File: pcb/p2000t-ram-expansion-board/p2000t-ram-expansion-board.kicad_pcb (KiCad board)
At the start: 2 copper layers, 110 x 68.1 mm, 28 parts, among them J1 EXPANSION BOARD, J2 POWER, J3 TERMINAL, U1 74HC04, U2 CY62256-70PC, U3 74HC00, U4 CY62256-70PC, U5 74HC688, U6 74HC32, U7 74HC173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

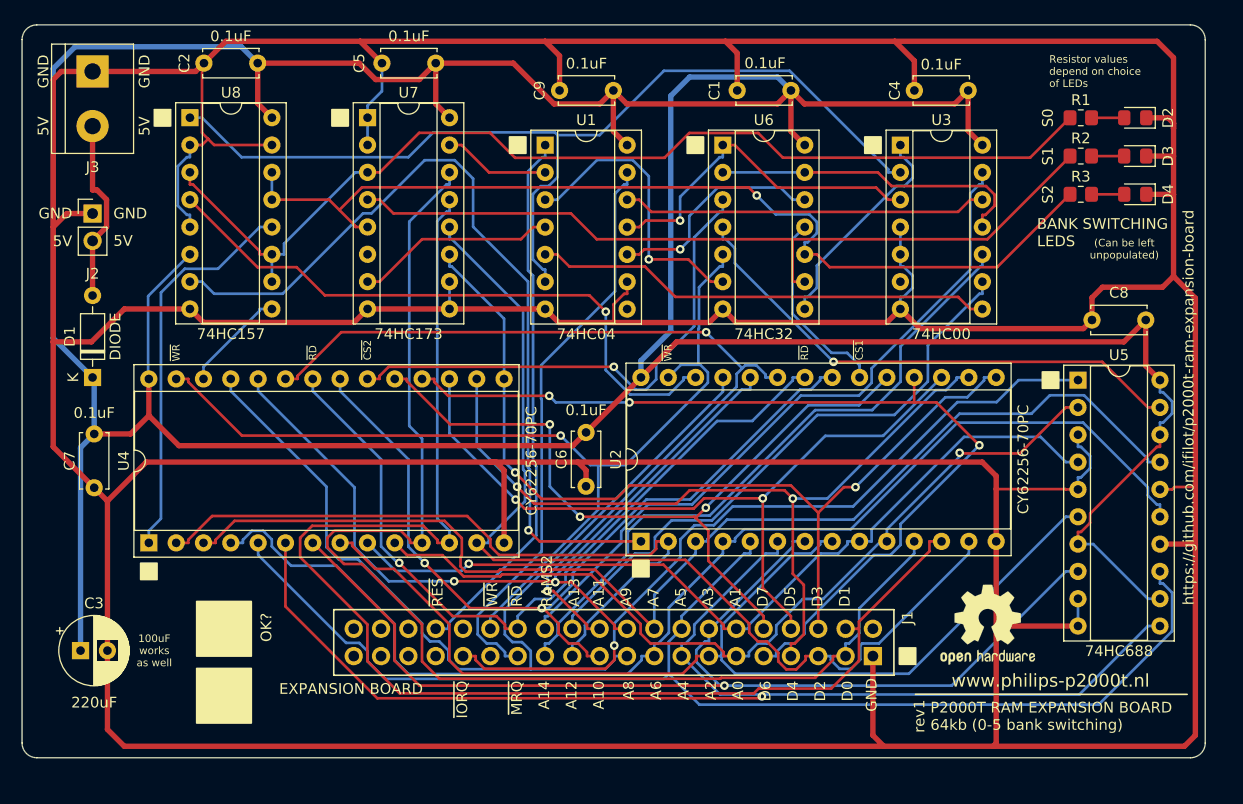
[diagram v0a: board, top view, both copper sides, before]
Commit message: Board revision 3 (#2)
* Adding 74HC245

* Fixing connection

* Revising board and fixing bugs

* Updating README.md

* Updating schematic

* Replacing images
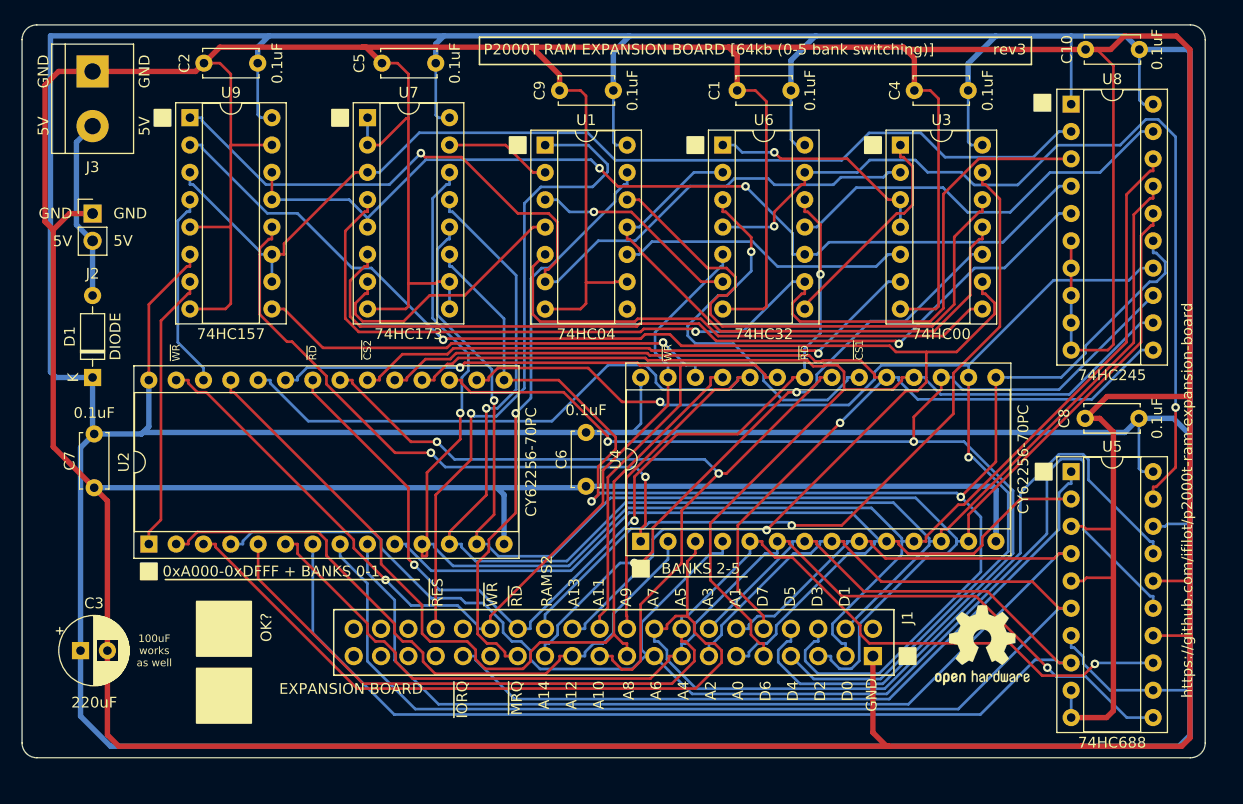
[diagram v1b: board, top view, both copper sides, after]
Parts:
- removed D2, D3, D4: LED, LED_SMD:LED_0805_2012Metric_Pad1.15x1.40mm_HandSolder
- removed R1, R2, R3: R, Resistor_SMD:R_0805_2012Metric_Pad1.20x1.40mm_HandSolder
- removed the REF** at (109.7, 77.6)
- added C10: 0.1uF, Capacitor_THT:C_Disc_D5.0mm_W2.5mm_P5.00mm, F.Cu at (123.8, 24.1)
- added REF**: OSHW-Logo2_9.8x8mm_SilkScreen, Symbol:OSHW-Logo2_9.8x8mm_SilkScreen, F.Cu at (109.2, 79.5)
- added REF**: OSHW-Logo2_9.8x8mm_SilkScreen, Symbol:OSHW-Logo2_9.8x8mm_SilkScreen, B.Cu at (109.2, 79.5)
- added U9: 74HC157, Package_DIP:DIP-16_W7.62mm_Socket, F.Cu at (35.6, 30.5)
- U8: value 74HC157 -> 74HC245; footprint Package_DIP:DIP-16_W7.62mm_Socket -> Package_DIP:DIP-20_W7.62mm_Socket
- moved U8 81.9 mm to (117.5, 29.2)
- moved U2 45.7 mm to (31.8, 70.1)
- moved U4 45.7 mm to (77.5, 69.8)
- moved C8 9.17 mm to (123.8, 58.4)
- moved U5 8.53 mm to (117.5, 63.4)
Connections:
- U1 pad 11: Net-(U1-Pad11) -> ~{REN}
- U3 pad 3: Net-(U1-Pad11) -> Net-(U3-Pad3)
- U3 pad 4: GND -> Net-(U3-Pad3)
- U3 pad 5: GND -> Net-(U1-Pad10)
- U3 pad 6: unconnected-(U3-Pad6) -> ~{CS1}
- U5 pad 19: Net-(U5-Pad19) -> ~{P=Q}
- U6 pad 1: Net-(U1-Pad11) -> Net-(U3-Pad3)
- U6 pad 11: ~{CS1} -> Net-(U6-Pad11)
- U6 pad 12: Net-(U1-Pad10) -> ~{RD}
- U6 pad 13: ~{REN} -> ~{P=Q}
- U6 pad 4: Net-(U5-Pad19) -> ~{P=Q}
- U7 pad 6: unconnected-(U7-Pad6) -> S3
- U8 pad 1: EO -> +5V
- U8 pad 10: S0 -> GND
- U8 pad 11: S0 -> D7
- U8 pad 12: A14_2 -> D6
- U8 pad 13: S2 -> D5
- U8 pad 14: S2 -> D4
- U8 pad 15: GND -> D3
- U8 pad 16: +5V -> D2
- U8 pad 2: GND -> S0
- U8 pad 3: S0 -> S1
- U8 pad 4: A13_1 -> S2
- U8 pad 5: GND -> S3
- U8 pad 6: +5V -> GND
- U8 pad 7: A14_1 -> GND
- U8 pad 9: A13_2 -> GND
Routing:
- net +5V: track 372.8 -> 561.2 mm
- net ~{P=Q}: track 0.00 -> 85.0 mm, vias 0 -> 2
- net S3: track 0.00 -> 79.9 mm, vias 0 -> 1
- net A13: track 55.5 -> 134.9 mm, vias 0 -> 2
- net D5: track 72.0 -> 125.4 mm
- net A14_1: track 78.5 -> 26.1 mm, vias 1 -> 0
- net D3: track 86.4 -> 136.6 mm
- net Net-(U5-Pad19): track 49.1 -> 0.00 mm, vias 1 -> 0
- net D2: track 94.2 -> 141.6 mm, vias 0 -> 1
- net A13_1: track 58.5 -> 18.4 mm, vias 1 -> 0
- net D4: track 75.6 -> 115.7 mm
- net GND: track 686.8 -> 726.2 mm
- net A1: track 79.5 -> 118.1 mm, vias 1 -> 0
- net Net-(U6-Pad11): track 0.00 -> 38.0 mm
- net ~{CS1}: track 17.9 -> 54.0 mm, vias 0 -> 1
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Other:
- board text added: "0xA000-0xDFFF + BANKS 0-1"
- board text added: "BANKS 2-5"
- board text added: "P2000T RAM EXPANSION BOARD [64kb (0-5 bank switching)]"
- board text added: "rev3"
- board text removed: "(Can be left unpopulated)"
- board text removed: "BANK SWITCHING LEDS"
- board text removed: "Resistor values depend on choice of LEDs"
- board text removed: "S0"
- board text removed: "S1"
- board text removed: "S2"
- board text removed: "rev1"
